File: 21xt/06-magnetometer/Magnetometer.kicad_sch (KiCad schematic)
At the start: 18 parts, among them J1 Conn_01x02, J3 Conn_01x02, U1 LIS3MDLTR, U2 BSS138, U3 LM3940IMPX-3.3, U4 BSS138

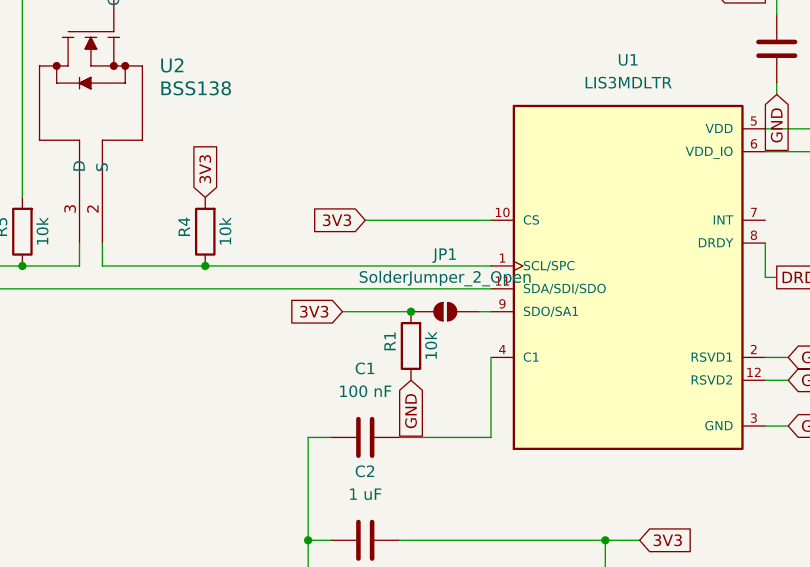
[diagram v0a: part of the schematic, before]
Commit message: magnetometer v4 - transistioned to 4 layer, mounting holes added
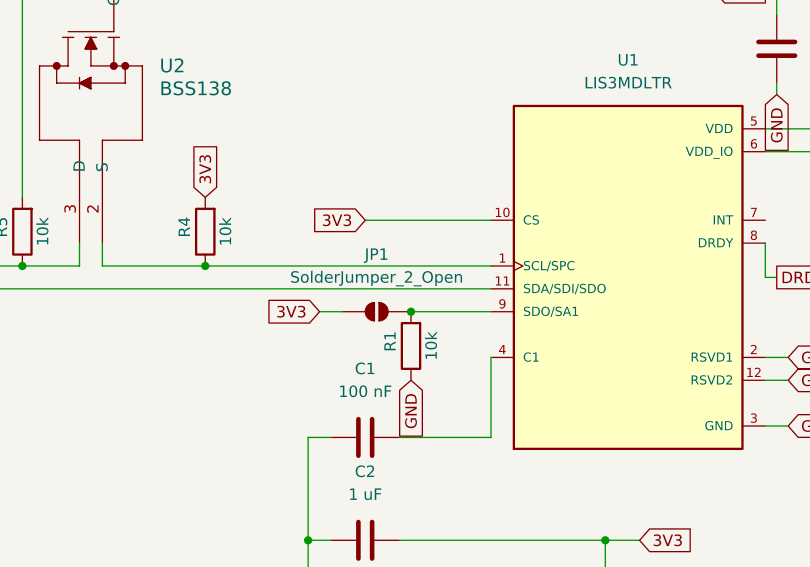
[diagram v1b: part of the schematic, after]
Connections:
- net 3V3: no longer R1.2
- net at JP1.2 (B), U1.9 (SDO/SA1): now also R1.2
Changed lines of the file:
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@@
+	)
+	(junction
+		(at 118.11 91.44)
+		(diameter 0)
+		(color 0 0 0 0)
 	)
 	(junction
@@
 	)
 	(junction
-		(at 118.11 91.44)
-		(diameter 0)
-		(color 0 0 0 0)
-	)
-	(junction
 		(at 43.18 88.9)
 		(diameter 0)
@@
 	(wire
 		(pts
+			(xy 118.11 91.44) (xy 127 91.44)
+		)
+		(stroke
+			(width 0)
+			(type default)
+		)
+	)
+	(wire
+		(pts
 			(xy 34.29 50.8) (xy 34.29 80.01)
 		)
@@
 	(wire
 		(pts
-			(xy 110.49 91.44) (xy 118.11 91.44)
+			(xy 107.95 91.44) (xy 110.49 91.44)
 		)
 		(stroke
@@
 		(pts
 			(xy 127 105.41) (xy 127 96.52)
-		)
-		(stroke
-			(width 0)
-			(type default)
-		)
-	)
-	(wire
-		(pts
-			(xy 125.73 91.44) (xy 127 91.44)
 		)
 		(stroke
@@
 	(global_label "3V3"
 		(shape input)
-		(at 110.49 91.44 180)
+		(at 107.95 91.44 180)
 		(fields_autoplaced yes)
 		(effects
@@
 		)
 		(property "Intersheetrefs" "${INTERSHEET_REFS}"
-			(at 103.9972 91.44 0)
+			(at 101.4572 91.44 0)
 			(effects
 				(font
@@
 	)
 	(symbol
+		(lib_id "Jumper:SolderJumper_2_Open")
+		(at 114.3 91.44 0)
+		(unit 1)
+		(exclude_from_sim yes)
+		(in_bom no)
+		(on_board yes)
+		(dnp no)
+		(fields_autoplaced yes)
+		(property "Reference" "JP1"
+			(at 114.3 85.09 0)
+			(effects
+				(font
+					(size 1.27 1.27)
+				)
+			)
+		)
+		(property "Value" "SolderJumper_2_Open"
+			(at 114.3 87.63 0)
+			(effects
+				(font
+					(size 1.27 1.27)
+				)
+			)
+		)
+		(property "Footprint" "MagnetometerFootprints:SolderJumper"
+			(at 114.3 91.44 0)
+			(effects
+				(font
+					(size 1.27 1.27)
+				)
+				(hide yes)
+			)
+		)
+		(property "Datasheet" "~"
+			(at 114.3 91.44 0)
+			(effects
+				(font
+					(size 1.27 1.27)
+				)
+				(hide yes)
+			)
+		)
+		(property "Description" "Solder Jumper, 2-pole, open"
+			(at 114.3 91.44 0)
+			(effects
+				(font
+					(size 1.27 1.27)
+				)
+				(hide yes)
+			)
+		)
+		(pin "2"
+		)
+		(pin "1"
+		)
+		(instances
+			(project "Magnetometer"
+				(path "/7aa67d3c-71d8-4831-bdde-1dffcd9aa2d3"
+					(reference "JP1")
+					(unit 1)
+				)
+			)
+		)
+	)
+	(symbol
 		(lib_id "Device:C")
 		(at 113.03 116.84 90)
@@
 					(unit 1)
 				)
-			)
-		)
-	)
-	(symbol
-		(lib_id "Jumper:SolderJumper_2_Open")
-		(at 121.92 91.44 0)
-		(unit 1)
-		(exclude_from_sim yes)
-		(in_bom no)
-		(on_board yes)
-		(dnp no)
-		(fields_autoplaced yes)
-		(property "Reference" "JP1"
-			(at 121.92 85.09 0)
-			(effects
-				(font
-					(size 1.27 1.27)
-				)
-			)
-		)
-		(property "Value" "SolderJumper_2_Open"
-			(at 121.92 87.63 0)
-			(effects
-				(font
-					(size 1.27 1.27)
-				)
-			)
-		)
-		(property "Footprint" "MagnetometerFootprints:SolderJumper"
-			(at 121.92 91.44 0)
-			(effects
-				(font
-					(size 1.27 1.27)
-				)
-				(hide yes)
-			)
-		)
-		(property "Datasheet" "~"
-			(at 121.92 91.44 0)
-			(effects
-				(font
-					(size 1.27 1.27)
-				)
-				(hide yes)
-			)
-		)
-		(property "Description" "Solder Jumper, 2-pole, open"
-			(at 121.92 91.44 0)
-			(effects
-				(font
-					(size 1.27 1.27)
-				)
-				(hide yes)
-			)
-		)
-		(pin "2"
-		)
-		(pin "1"
-		)
-		(instances
-			(project ""
-				(path "/7aa67d3c-71d8-4831-bdde-1dffcd9aa2d3"
-					(reference "JP1")
-					(unit 1)
-				)

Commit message: magnetometer v4 - added 3D symbols to footprints, uploading downloaded footprints, symbols, and 3D models
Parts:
- CR2: footprint MagnetometerFootprints:1KSMB24A -> MagnetometerFootprints:1KSMBSeries_LTF
- U1: footprint MagnetometerFootprints:XDCR_LIS3MDLTR -> MagnetometerFootprints:LIS3MDLTR
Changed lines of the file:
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@@
 			)
 		)
-		(property "Footprint" "MagnetometerFootprints:XDCR_LIS3MDLTR"
+		(property "Footprint" "MagnetometerFootprints:LIS3MDLTR"
 			(at 142.24 86.36 0)
 			(effects
@@
 			)
 		)
-		(property "Footprint" "MagnetometerFootprints:1KSMB24A"
+		(property "Footprint" "MagnetometerFootprints:1KSMBSeries_LTF"
 			(at 203.2 45.72 0)
 			(effects

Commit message: magnetometer v6 -changed LM390 to TPS7933, caps and resistors to 0402, padded mounting holes, teardrops
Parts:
- removed U3: LM3940IMPX-3.3, MagnetometerFootprints:LM3940, symbol Regulator:LM3940IMPX-3.3
- added C6: 2.2 uF, Capacitor_SMD:C_0402_1005Metric, symbol Device:C
- added U5: TPS79333DBVRG4Q1, MagnetometerFootprints:DBV5_TEX, symbol MagnetometerSymbols:TPS79333DBVRG4Q1
- C1, C2, C3: footprint Capacitor_SMD:C_0201_0603Metric -> Capacitor_SMD:C_0402_1005Metric
- C4: value 33 uF -> 0.1 uF; footprint Capacitor_SMD:C_0201_0603Metric -> Capacitor_SMD:C_0402_1005Metric
- C5: value .47 uF -> 0.01 uF; footprint Capacitor_SMD:C_0201_0603Metric -> Capacitor_SMD:C_0402_1005Metric
- R1, R2, R3, R4, R5: footprint Resistor_SMD:R_0201_0603Metric -> Resistor_SMD:R_0402_1005Metric
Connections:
- net 3V3: now also C6.1, U5.5 (OUT); no longer C5.1
- net 5V: now also U5.1 (IN), U5.3 (EN)
- net GND: now also C6.2, U5.2 (GND)
- net SDA: no longer R2.1, U1.11 (SDA/SDI/SDO), U4.2 (S)
- new net: R2.1, U1.11 (SDA/SDI/SDO), U4.2 (S)
- new net: C5.1, U5.4 (BYPASS)
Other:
- moved on the sheet: CR2
